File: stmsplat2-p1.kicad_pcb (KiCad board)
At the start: 2 copper layers, 100 x 100 mm, 113 parts, among them J1 C11_2X36, J10 Conn_01x03_Male, J11 Conn_01x02_Male, J12 Conn_01x04_Male, J13 Conn_01x04_Male, J14 Conn_01x02, J15 Conn_01x02, J16 Screw_Terminal_01x03, J17 Screw_Terminal_01x02, J2 C12_2X36, J3 Conn_01x04_Male, J4 Conn_01x04_Male, J5 Conn_Coaxial, J6 Conn_01x04_Male, J7 Conn_01x04_Male, J8 Conn_01x04_Male, J9 Conn_01x03_Male, Q1 BSS138LT1G, U1 ublox_chinese_PCB_module, U10 XCVR_E30-400M20S (Si4463), U11 3115_module, U2 ESP-C3-13U, U3 SST25VF032B, U4 48L512-48LM01, U5 Opamp_Quad_MCP6024, U6 E180-ZG120A, U7 AZ1084C, U8 MCP6S93-X_UN, U9 DS2485

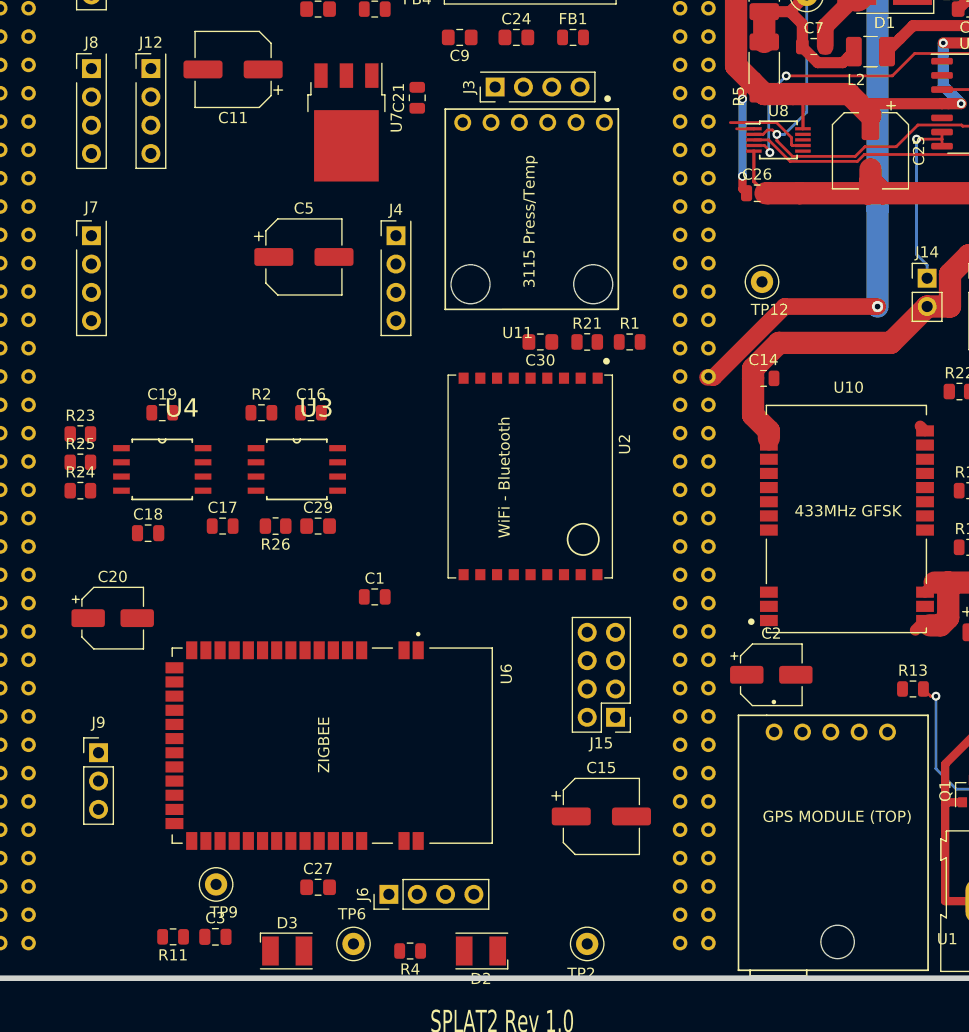
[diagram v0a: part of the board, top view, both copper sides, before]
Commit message: SPI2<->SPI3. Different placement. Routed, but may have other errors
Swapped SPI2 and SPI3 and have added termination for SPI2 (which may not be needed)/ Moved RAM/ROM components close to the connector
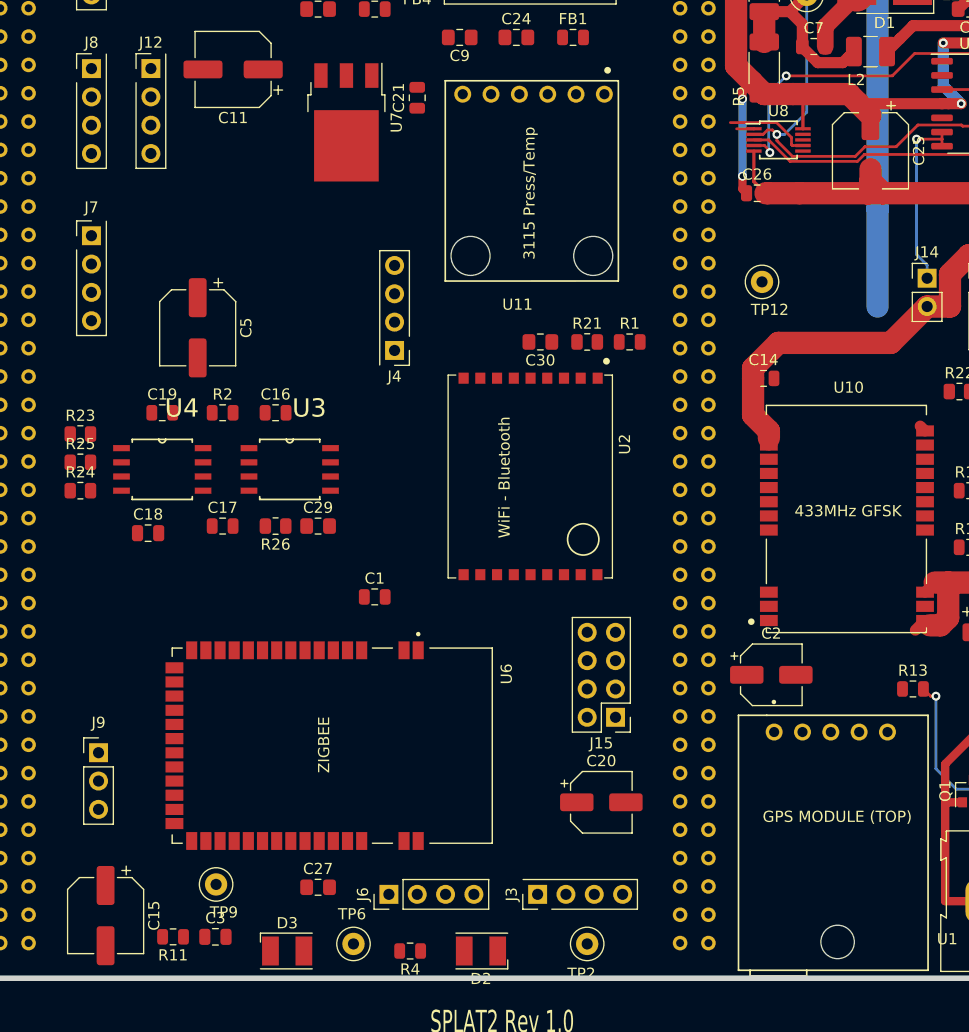
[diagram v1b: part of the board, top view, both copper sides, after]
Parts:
- moved J3 72.5 mm to (103.5, 158.1)
- moved C20 46.8 mm to (109.2, 149.9)
- moved C15 45.3 mm to (64.8, 160.0), turned to 270 degrees
- moved C5 11.4 mm to (73.0, 107.3), turned to 270 degrees
- moved J4 10.3 mm to (90.7, 109.3), turned to 180 degrees
- moved R2 3.48 mm to (75.3, 114.9)
- moved C16 3.17 mm to (80.0, 114.9)
- moved U11 2.54 mm to (110.5, 102.9)
- moved U3 0.64 mm to (81.3, 120.0)
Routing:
- net GNDA: track 215.5 -> 197.6 mm, vias 1 -> 0
